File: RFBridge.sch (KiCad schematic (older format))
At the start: 8 parts, among them P5 USB_B

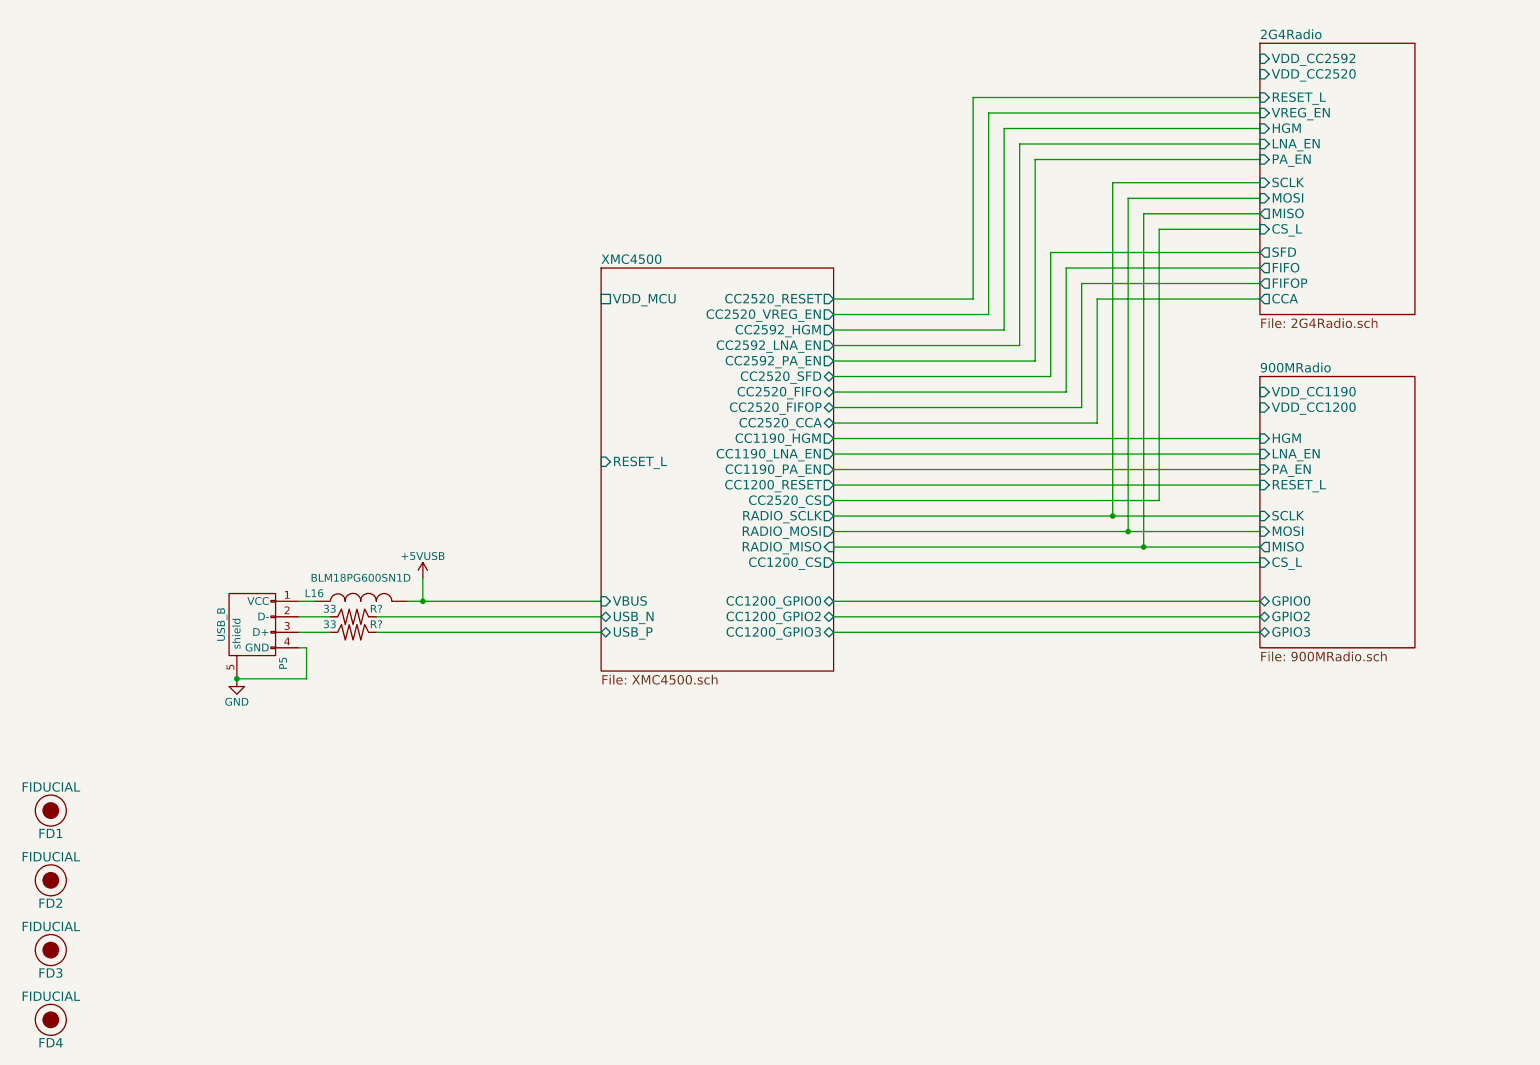
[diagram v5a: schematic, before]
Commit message: Added 3.3V LDO
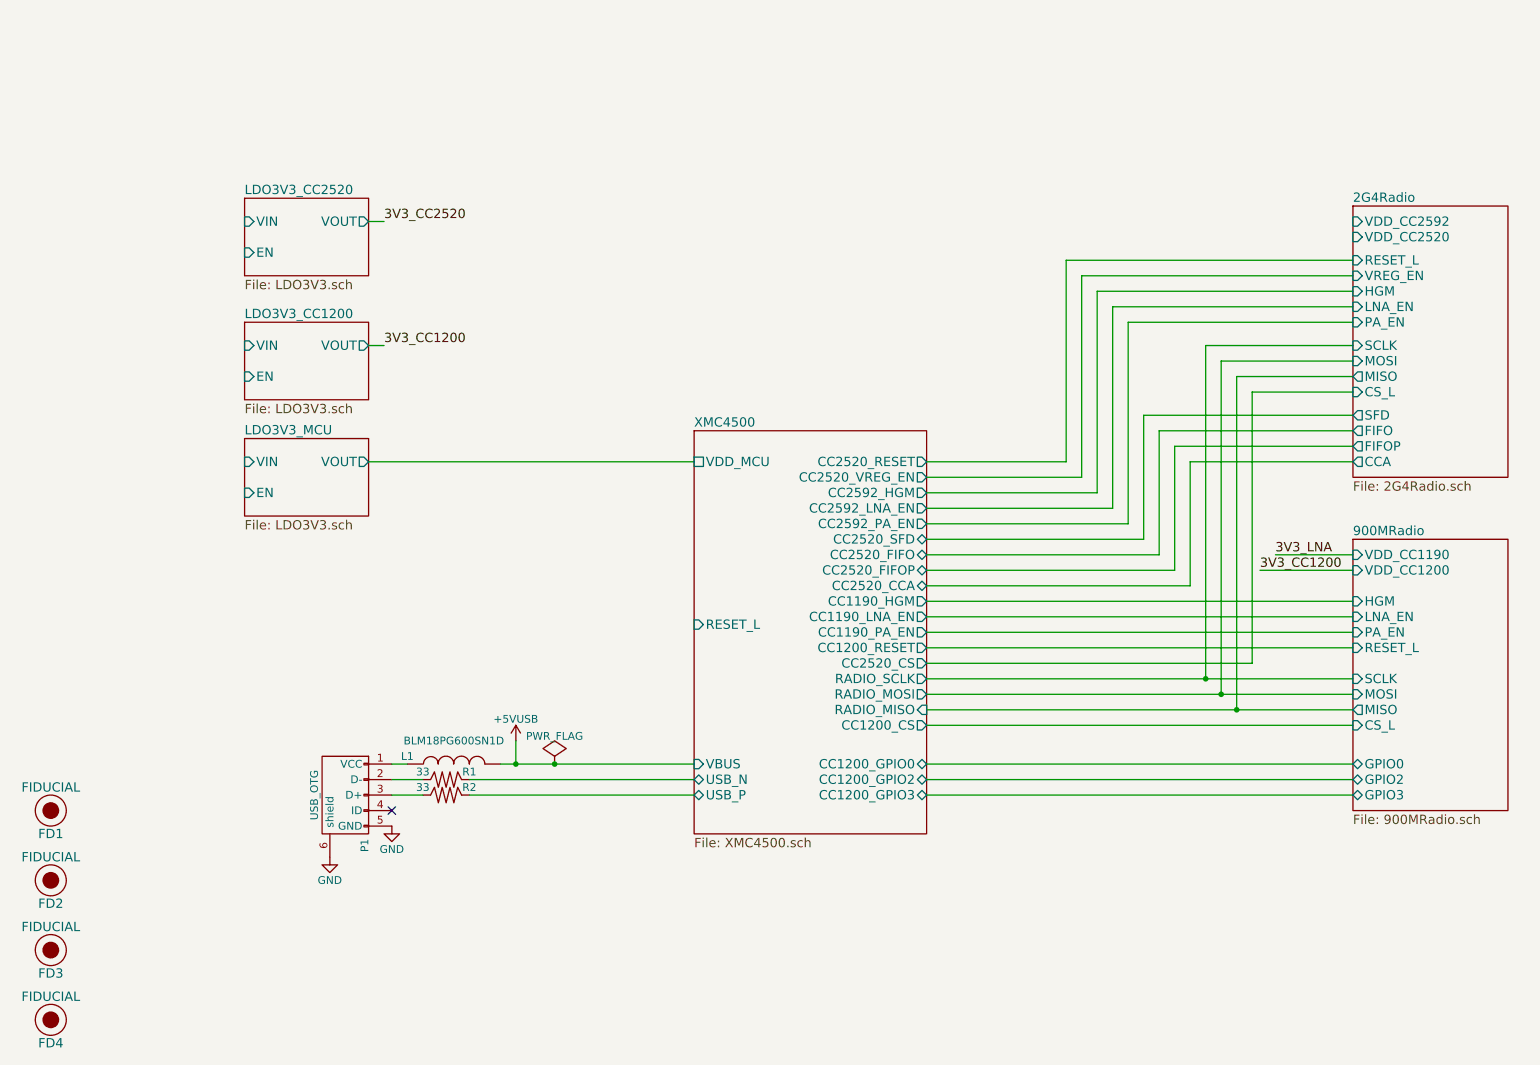
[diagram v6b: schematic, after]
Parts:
- removed P5: USB_B, Connect:USB_Micro-B, symbol USB_B
- added P1: USB_OTG, symbol USB_OTG
- R1, R2: renamed from R?; footprint (none) -> Resistors_SMD:R_0402
- renumbered L16 to L1
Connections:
- net GND: now also P1.5 (GND), P1.6 (shield)
- net at L1.1: now also P1.1 (VCC)
- net at R1.2: now also P1.2 (D-)
- net at R2.2: now also P1.3 (D+)
- no-connect marks 0 -> 1
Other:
- moved on the sheet: L1, R1, R2

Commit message: Added barrel jack and ideal diode circuit
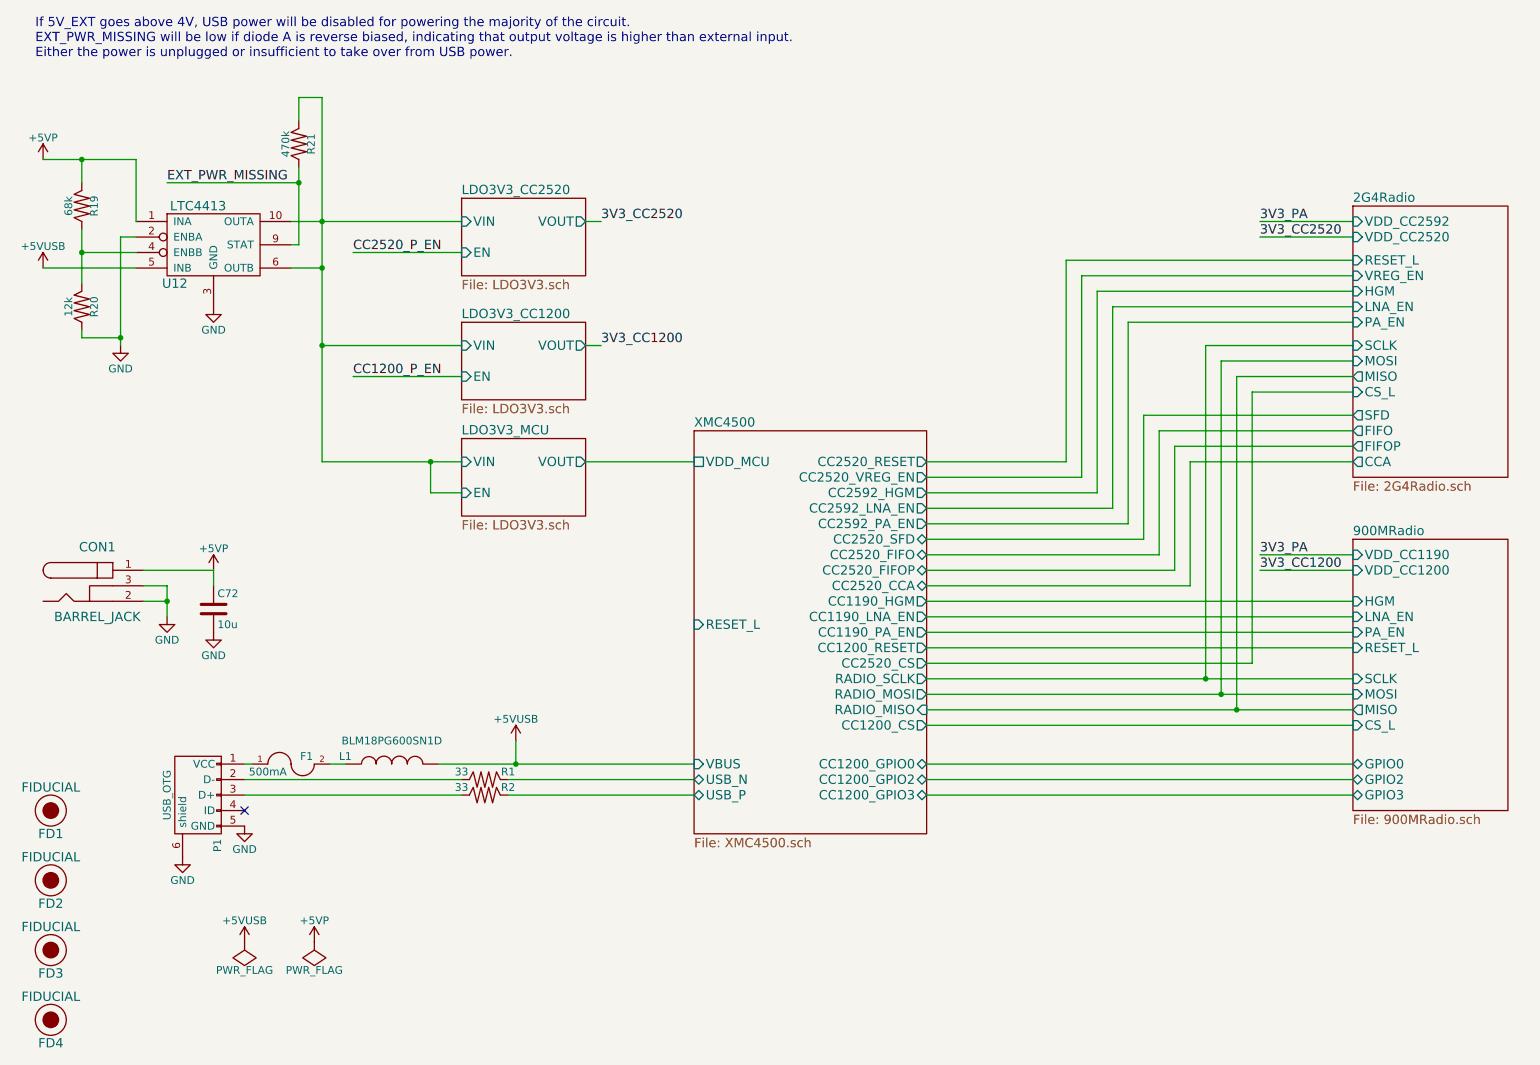
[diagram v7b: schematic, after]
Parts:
- added C72: 10u, Capacitors_SMD:C_0603, symbol C
- added CON1: BARREL_JACK, Connect:BARREL_JACK, symbol BARREL_JACK
- added F1: 500mA, Resistors_SMD:R_0402, symbol FUSE
- added R19: 68k, Resistors_SMD:R_0402, symbol R
- added R20: 12k, Resistors_SMD:R_0402, symbol R
- added R21: 470k, Resistors_SMD:R_0402, symbol R
- added U12: LTC4413, Housings_DFN_QFN:DFN-10-1EP_3x3mm_Pitch0.5mm, symbol LTC4413
- P1: footprint (none) -> Connect:USB_Micro-B
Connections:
- net +5VUSB: now also U12.5 (INB)
- net GND: now also C72.2, CON1.2, CON1.3, R20.2, U12.11 (GND), U12.2 (ENBA), U12.3 (GND)
- net LDO3V3_CC1200/VIN: now also R21.1, U12.10 (OUTA), U12.6 (OUTB)
- net at L1.1: now also F1.2; no longer P1.1 (VCC)
- new net: F1.1, P1.1 (VCC)
- new net: R19.2, R20.1, U12.4 (ENBB)
- new net +5VP: C72.1, CON1.1, R19.1, U12.1 (INA)
- new net EXT_PWR_MISSING: R21.2, U12.9 (STAT)
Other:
- note added: "If 5V_EXT goes above 4V, USB power will be disabled for powering the majority of the circuit. \nEXT_PWR_MISSING will be low if diode A is reverse biased, indicating that output voltage is higher than external input.\nEither the power is unplugged or insufficient to take over from USB power."
- moved on the sheet: L1, P1, R1, R2
